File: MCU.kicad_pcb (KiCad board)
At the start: 4 copper layers, 110.3 x 131 mm, 94 parts, among them J1 HSEC8-150-01-X-RA-X, J10 Conn_02x10_Odd_Even, J11 Conn_01x10, J12 Conn_01x10, J13 Conn_01x10, J14 Conn_01x10, J15 Conn_01x02, J16 Conn_02x10_Odd_Even, J17 Conn_02x30_Counter_Clockwise, J18 Conn_01x10, J19 Conn_01x10, J2 Barrel_Jack_MountingPin, J20 Conn_01x02, J21 Conn_02x10_Odd_Even, J22 Conn_01x02, J23 Conn_01x02, J32 Conn_01x02, J4 Conn_02x30_Counter_Clockwise, J5 Conn_02x10_Odd_Even, J6 Conn_01x02, J7 Conn_01x10, J8 Conn_01x10, J9 Conn_01x02, U1 TPS76333, U11 TPS76333, U12 TXB0104RUT, U14 TPS76333, U2 TXB0104RUT, U3 LMR36510ADDA, U6 TXB0104RUT, U8 TPS76333, U9 TXB0104RUT

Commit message: Validated for prod
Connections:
- J4 pad 39: PE10_EXTI10 -> unconnected-(J4-Pin_39-Pad39)
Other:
- board text added: "24PG"
- board text added: "3V3"
- board text added: "CLK"
- board text added: "CTKCD"
- board text added: "EN"
- board text added: "INRSH"
- board text added: "ISOEN"
- board text added: "ISOHD"
- board text added: "ISOST"
- board text added: "LEMDS"
- board text added: "LEMUS"
- board text added: "MISO"
- board text added: "MOSI"
- board text added: "NCS"
- board text added: "OPCL"
- board text added: "OVCF"
- board text added: "PG"
- board text added: "SDMOS"
- board text added: "SPR"
- board text added: "SSRCTL"
- board text added: "T1"
- board text added: "T2"
- board text added: "VACT"
- board text added: "VCTK"
- board text added: "VDS"
- board text added: "VHERM"
- board text added: "VM1"
- board text added: "VM2"
- board text added: "VTMP"
- board text added: "VUS"

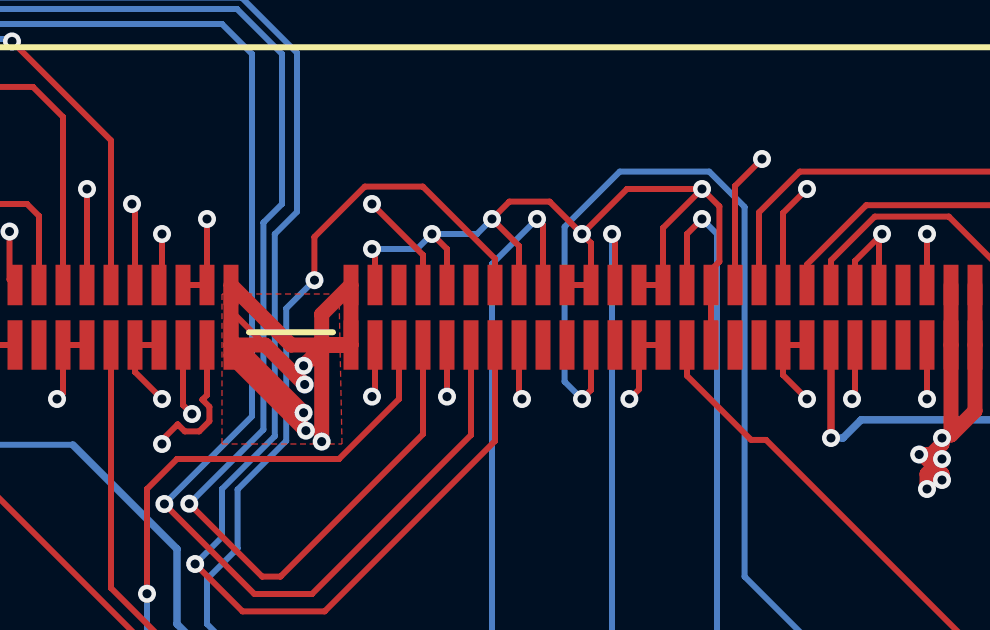
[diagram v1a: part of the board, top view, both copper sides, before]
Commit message: breakout typo
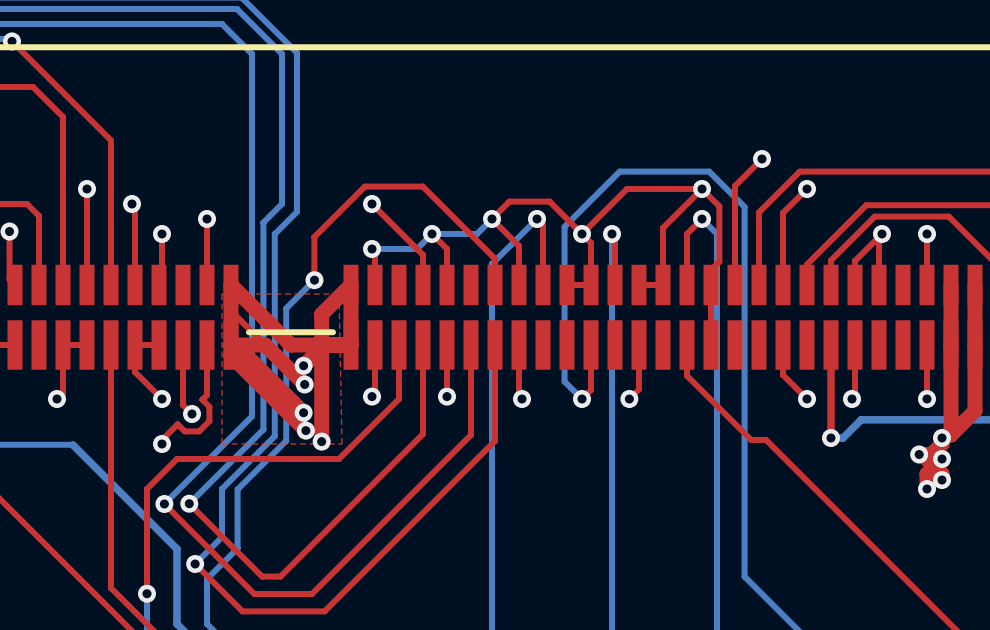
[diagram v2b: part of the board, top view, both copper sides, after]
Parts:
- R89: value 25.5k -> 25k5
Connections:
- J1 pad 16: A0V -> unconnected-(J1-Pad16)
- J1 pad 28: A0V -> unconnected-(J1-Pad28)
- J1 pad 59: A0V -> unconnected-(J1-Pad59)
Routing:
- net P5VAN: track 366.8 -> 436.8 mm
- net A0V: track 250.5 -> 248.1 mm

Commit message: Go vertical + BOM
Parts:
- J1: value HSEC8-150-01-X-RA-X -> HSEC8-150-01-X-DV-A; footprint kicad_jlcpcb_hil_mcu_ep2:SAMTEC_HSEC8-150-01-X-RA-X -> Connector_Samtec_HSEC8:Samtec_HSEC8-150-01-X-DV-A_2x50_P0.8mm_Pol27_Socket_AlignmentPins
- moved J1 4.63 mm to (108.7, 33.2), turned to 0 degrees
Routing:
- net DS_MISO: track 372.6 -> 449.5 mm, vias 2 -> 1
- net DS_NCS_C2: track 125.9 -> 189.7 mm, vias 2 -> 4
- net DS_NCS_C1: track 94.7 -> 153.0 mm, vias 1 -> 3
- net OPCL_DS: track 109.7 -> 160.1 mm, vias 2 -> 3
- net CTANK_CH_DISCH: track 77.1 -> 122.5 mm
- net ISOSW_OF_ST: track 200.6 -> 159.9 mm
- net ISOSW_INRUSH_CMD: track 170.4 -> 133.9 mm
- net SDMOS: track 113.8 -> 149.3 mm, vias 0 -> 2
- net PADLOCK_OF: track 241.2 -> 209.1 mm
- net US_MOSI: track 128.8 -> 157.8 mm
- net DS_MOSI: track 177.1 -> 204.6 mm, vias 0 -> 2
- net US_NCS_C2: track 125.2 -> 151.6 mm
- net V_HERMES: track 138.8 -> 164.4 mm, vias 1 -> 3
- net US_NCS_C1: track 76.8 -> 102.2 mm
- net VPS_P24V_PG: track 93.2 -> 117.6 mm
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- added copper zone on B.Cu, net A0V
- added copper zone on F.Cu, net A0V
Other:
- board size 110.3 x 131 mm -> 110.4 x 127 mm

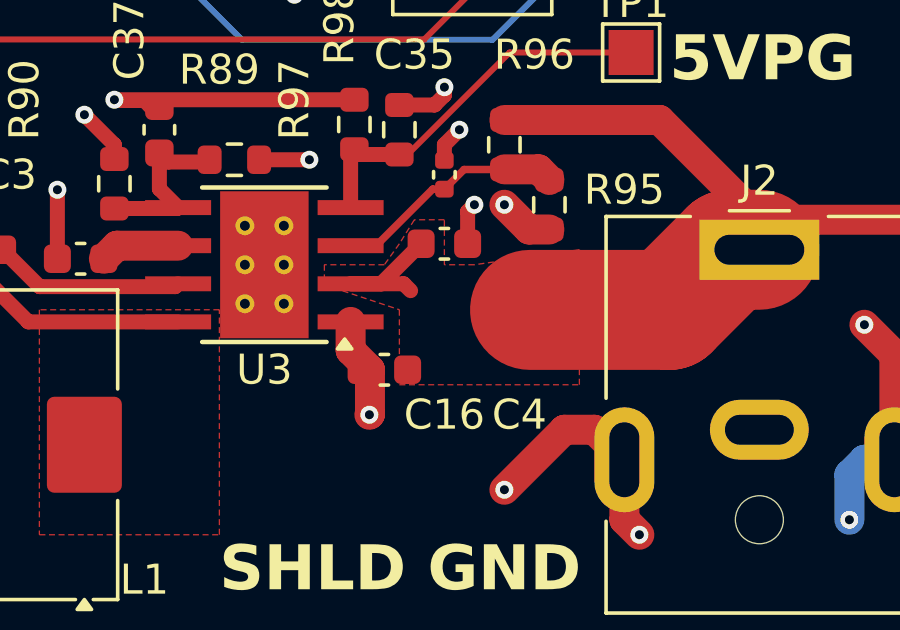
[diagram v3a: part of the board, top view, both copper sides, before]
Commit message: Production JLCPCB via France
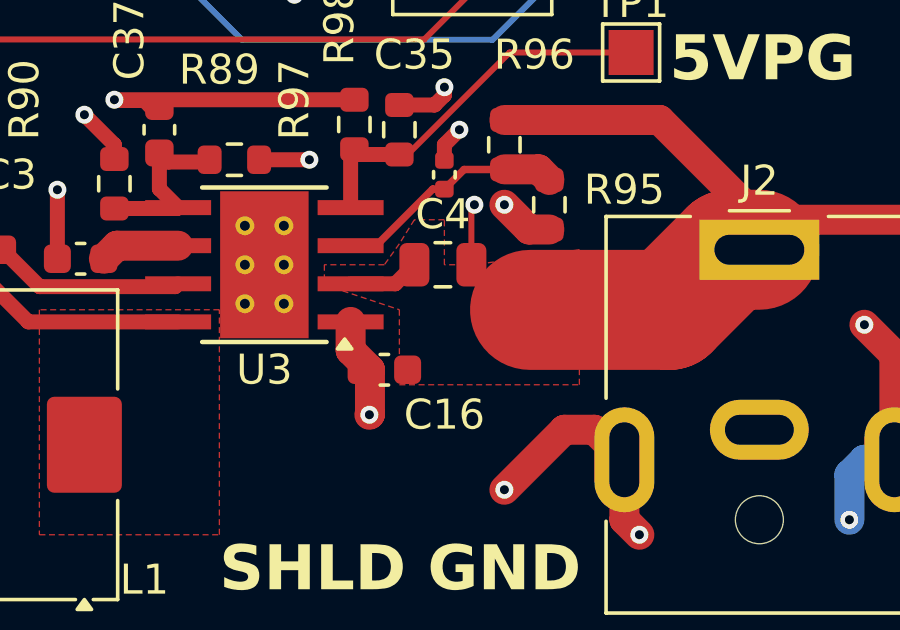
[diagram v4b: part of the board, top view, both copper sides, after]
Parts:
- C4: footprint Capacitor_SMD:C_0603_1608Metric -> Capacitor_SMD:C_0805_2012Metric
- moved C4 0.70 mm to (127.0, 141.0)
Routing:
- net P24V: track 172.5 -> 169.9 mm
- net A0V: track 236.2 -> 236.8 mm
